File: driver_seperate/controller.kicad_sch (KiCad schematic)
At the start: 17 parts, among them IC1 MCT8316Z0TQRGFRQ1, J2 Motor

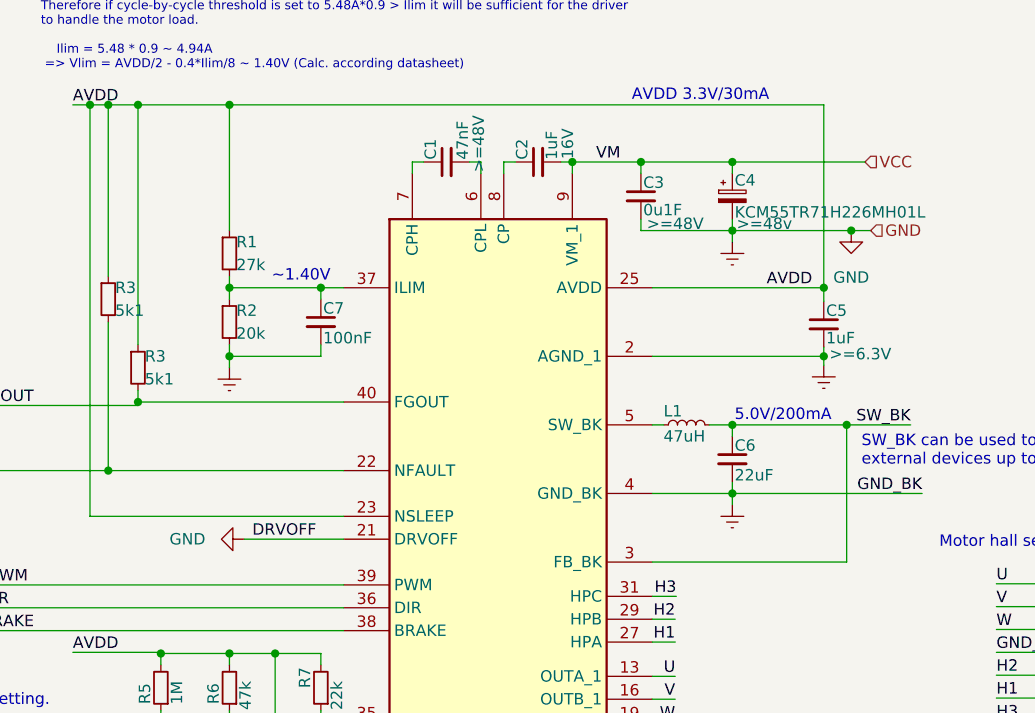
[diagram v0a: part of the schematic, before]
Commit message: Remove unused from schematic
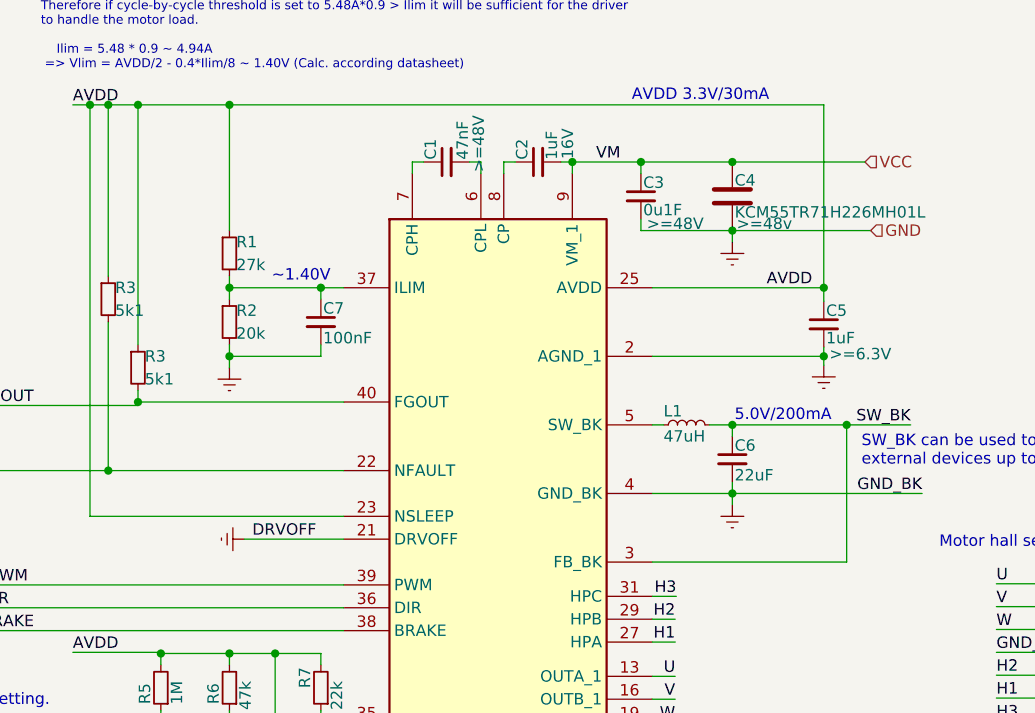
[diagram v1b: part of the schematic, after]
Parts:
- C4: symbol Device:C_Polarized_Small -> Device:C
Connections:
- net GND renamed GNDREF
